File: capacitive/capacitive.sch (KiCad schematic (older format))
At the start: 63 parts, among them J101 UL, J102 UART, J103 SWD, J104 TX_PADS, J105 RX_PAD, J106 POWER, J107 UR, J108 LL, J109 LR, Q101 RU1C002ZPTCL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

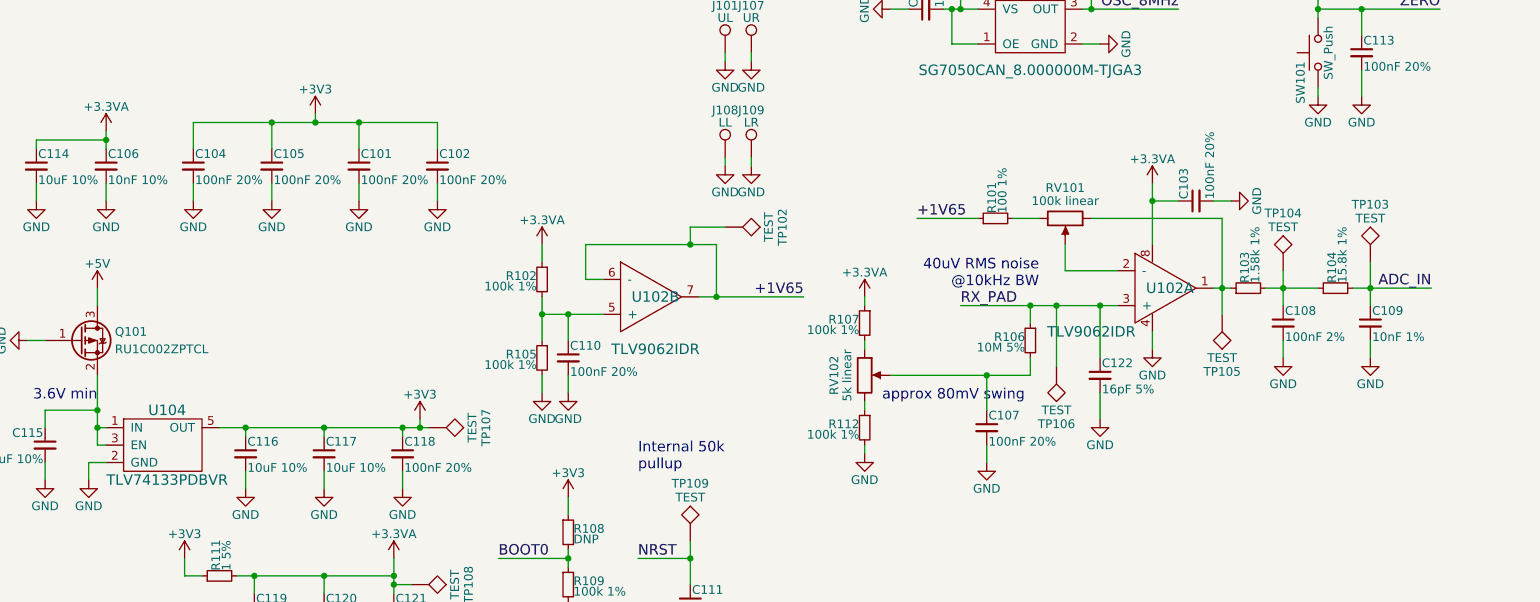
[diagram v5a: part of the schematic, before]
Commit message: Fix mouser BOM generation, add in notes from current testing
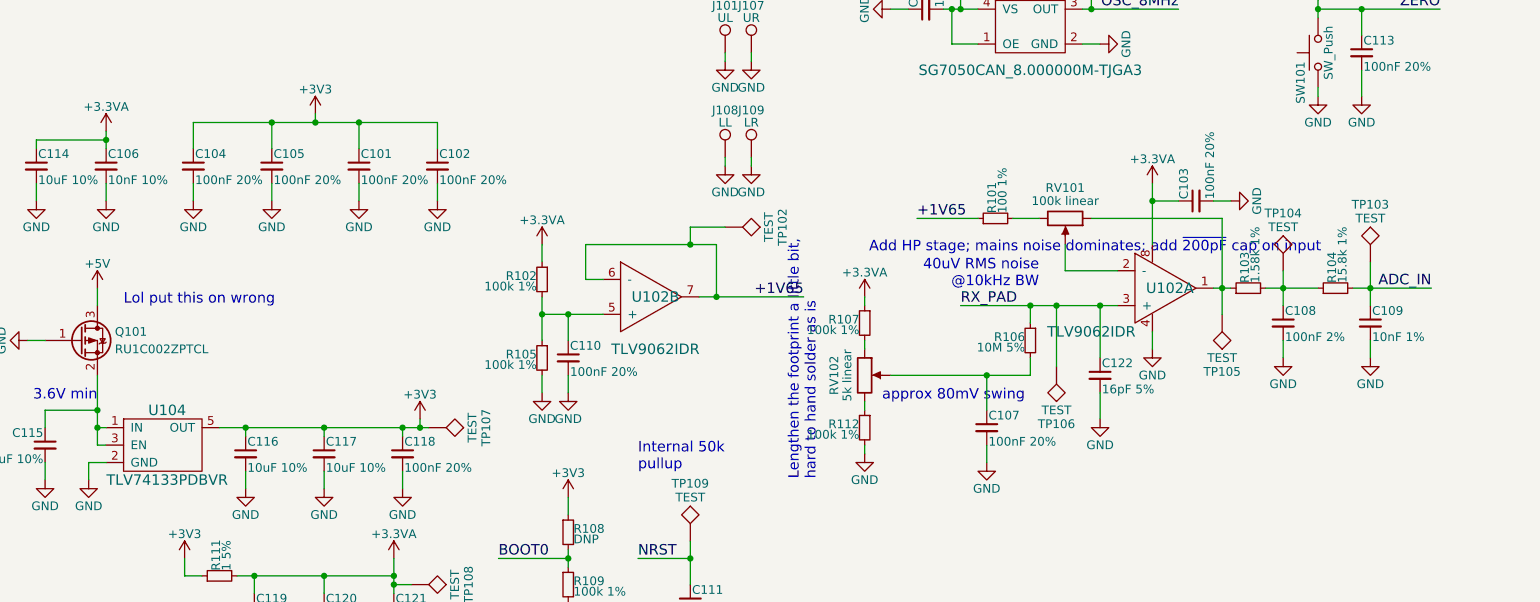
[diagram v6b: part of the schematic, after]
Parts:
- C122: Mouser 963-TMK042CG160JC-W -> 81-GCM1885C1H160FA6J
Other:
- note added: "Add HP stage; mains noise dominates; add ~200pF cap on input"
- note added: "Lengthen the footprint a little bit,\nhard to hand solder as is"
- note added: "Lol put this on wrong"
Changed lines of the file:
@@
 F 2 "Capacitors_SMD:C_0603_HandSoldering" H 8900 5850 50  0001 C CNN
 F 3 "" H 8900 5850 50  0001 C CNN
-F 4 "963-TMK042CG160JC-W" H 8900 5850 60  0001 C CNN "Mouser"
+F 4 "81-GCM1885C1H160FA6J" H 8900 5850 60  0001 C CNN "Mouser"
 	1    8900 5850
 	1    0    0    -1
@@
 Wire Wire Line
 	8900 5950 8900 6100
+Text Notes 3300 5450 0    60   ~ 0
+Lol put this on wrong
+Text Notes 7275 6450 1    60   ~ 0
+Lengthen the footprint a little bit,\nhard to hand solder as is
+Text Notes 7575 5150 0    60   ~ 0
+Add HP stage; mains noise dominates; add ~200pF cap on input
 $EndSCHEMATC

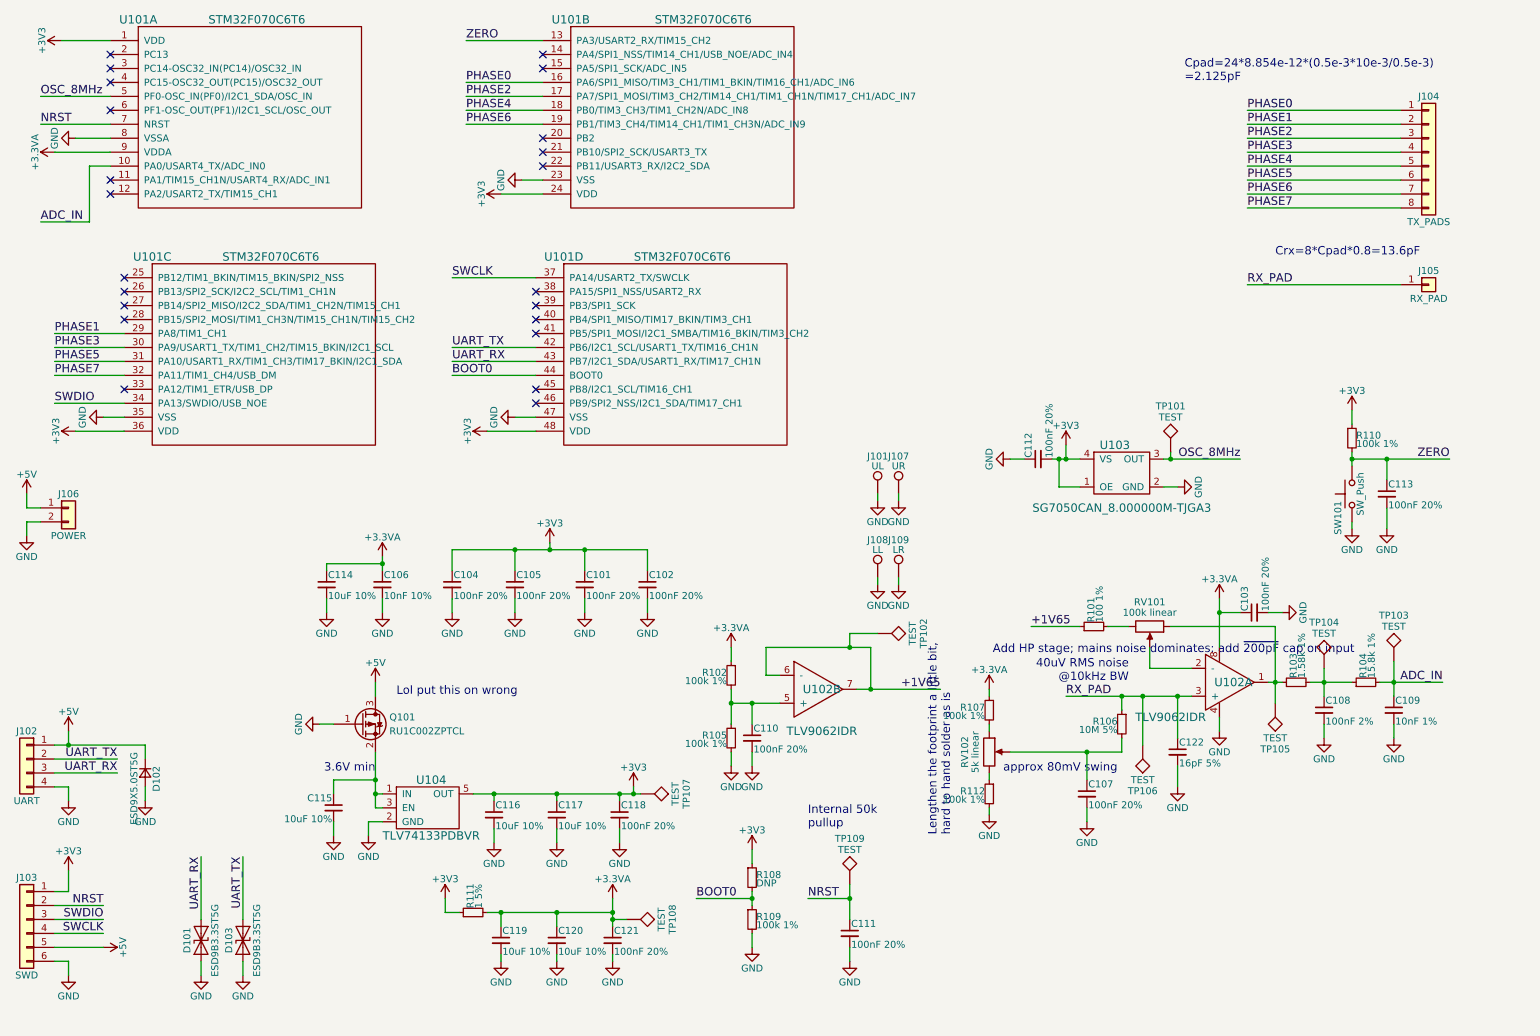
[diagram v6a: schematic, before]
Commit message: Add in some spots to experiment with filtering in the future
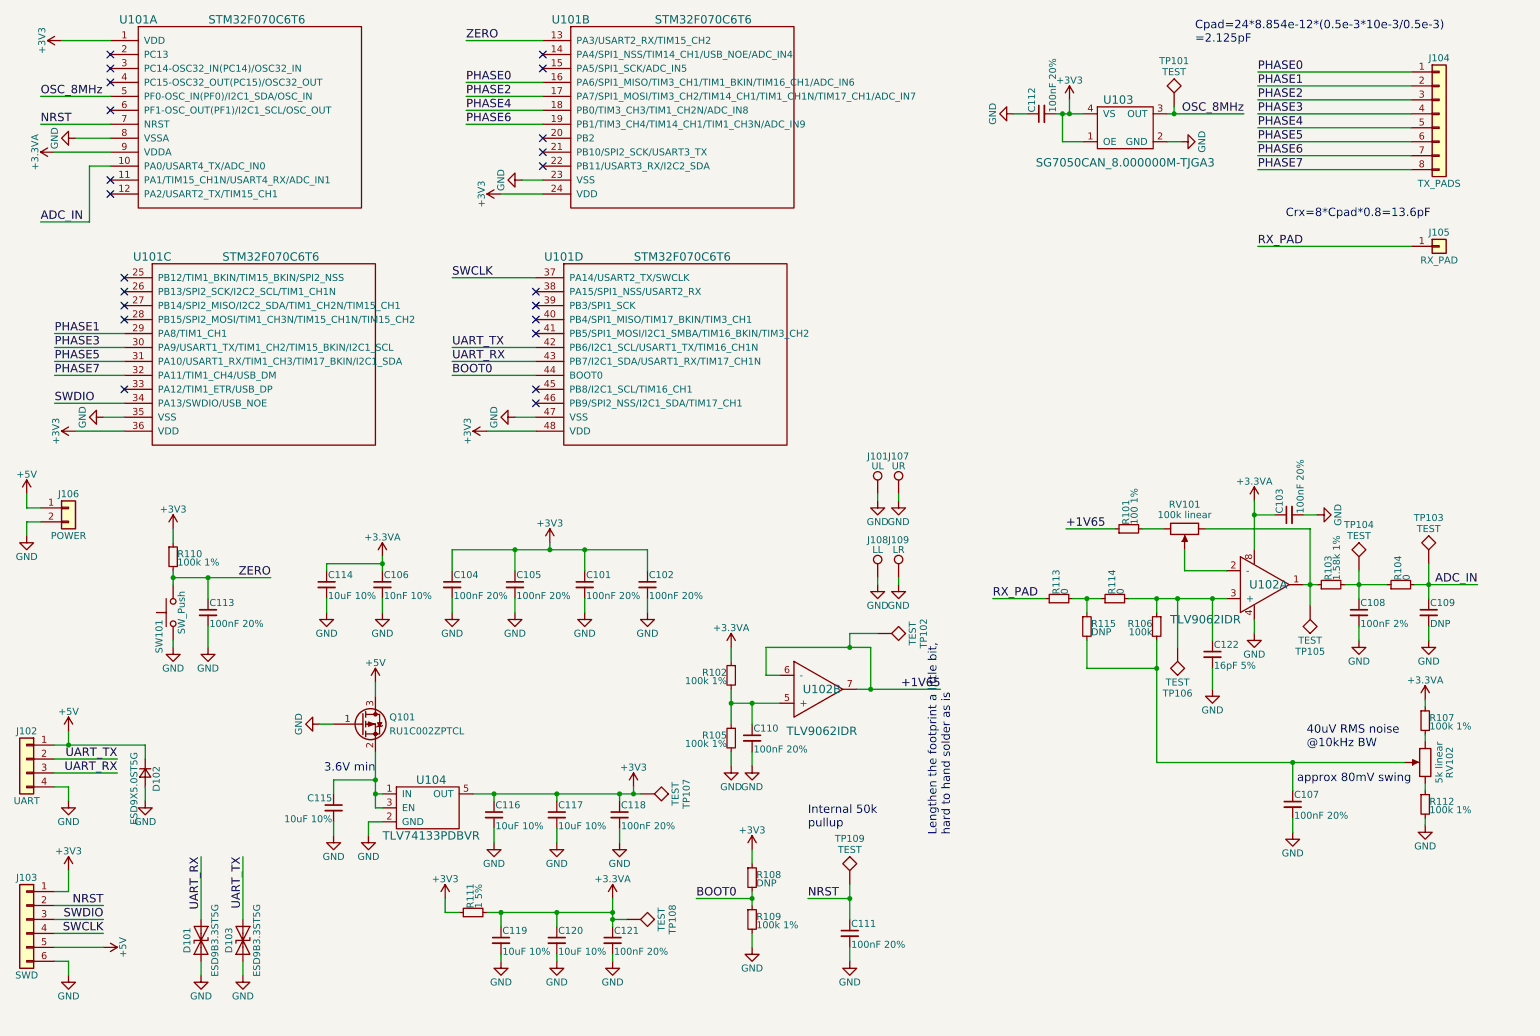
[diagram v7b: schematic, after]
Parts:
- added R113, R114: 0, Resistors_SMD:R_0805_HandSoldering, symbol R_Small
- added R115: DNP, Resistors_SMD:R_0603_HandSoldering, symbol R_Small
- C109: value 10nF 1% -> DNP
- R104: value 15.8k 1% -> 0; footprint Resistors_SMD:R_1206_HandSoldering -> Resistors_SMD:R_0805_HandSoldering; Mouser 667-ERJ-8ENF1582V -> 71-CRCW12060000Z0EAC
- R106: value 10M 5% -> 100k; footprint Resistors_SMD:R_0603_HandSoldering -> (none); Mouser 652-CR0603JW-106ELF -> (none)
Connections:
- net RX_PAD: now also R113.1; no longer C122.1, R106.1, TP106.1, U102.3 (+)
- net at C107.1, R106.2, RV102.2: now also R115.2
- new net: C122.1, R106.1, R114.2, TP106.1, U102.3 (+)
- new net: R113.2, R114.1, R115.1
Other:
- note removed: "Add HP stage; mains noise dominates; add ~200pF cap on input"
- note removed: "Lol put this on wrong"
- moved on the sheet: C103, C107, C108, C109, C112, C113, C122, J104, J105, R101, R103, R106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

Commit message: Update schematic a bit
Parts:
- C109: Mouser 81-GRM2195C1H103FA1D -> NoPart
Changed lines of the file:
@@
 F 2 "Capacitors_SMD:C_0805_HandSoldering" H 10700 4850 50  0001 C CNN
 F 3 "" H 10700 4850 50  0001 C CNN
-F 4 "81-GRM2195C1H103FA1D" H 10700 4850 60  0001 C CNN "Mouser"
+F 4 "NoPart" H 10700 4850 60  0001 C CNN "Mouser"
 	1    10700 4850
 	1    0    0    -1
